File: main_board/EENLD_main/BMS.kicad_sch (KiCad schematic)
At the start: 20 parts, among them J201 Conn_01x02_Socket, Q201 AO3401A, SW201 SW_SPST, U201 TPS25200DRVR

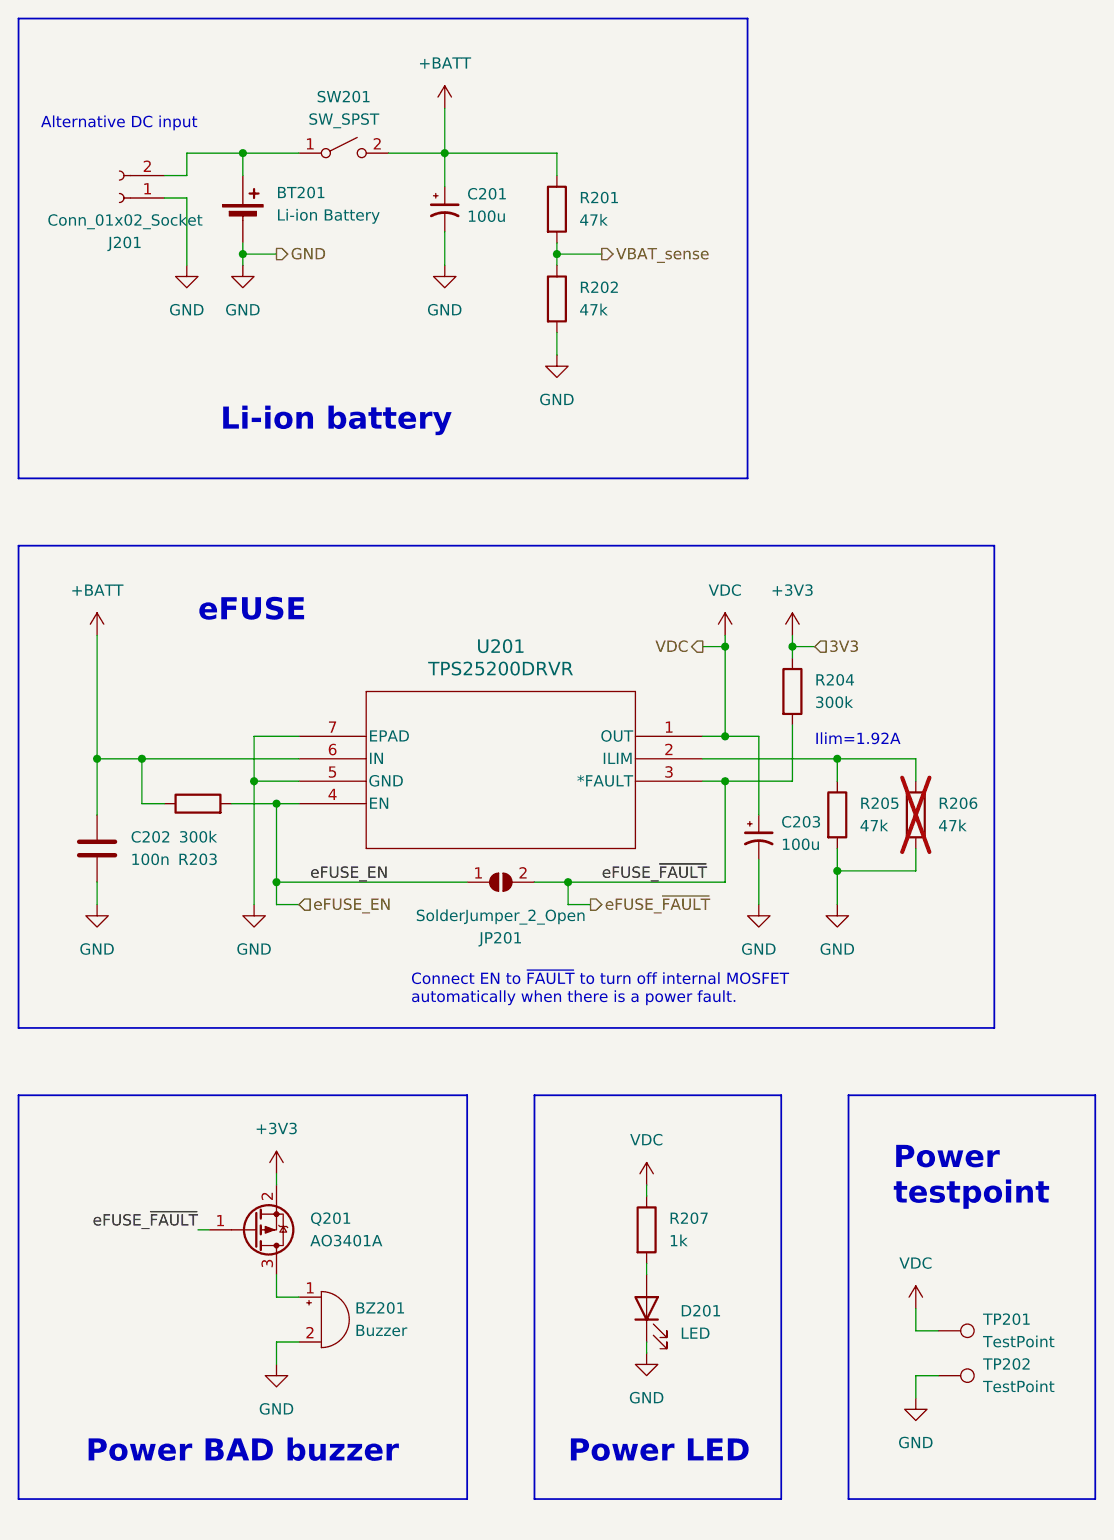
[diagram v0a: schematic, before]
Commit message: Finished PCB layout v0.1.
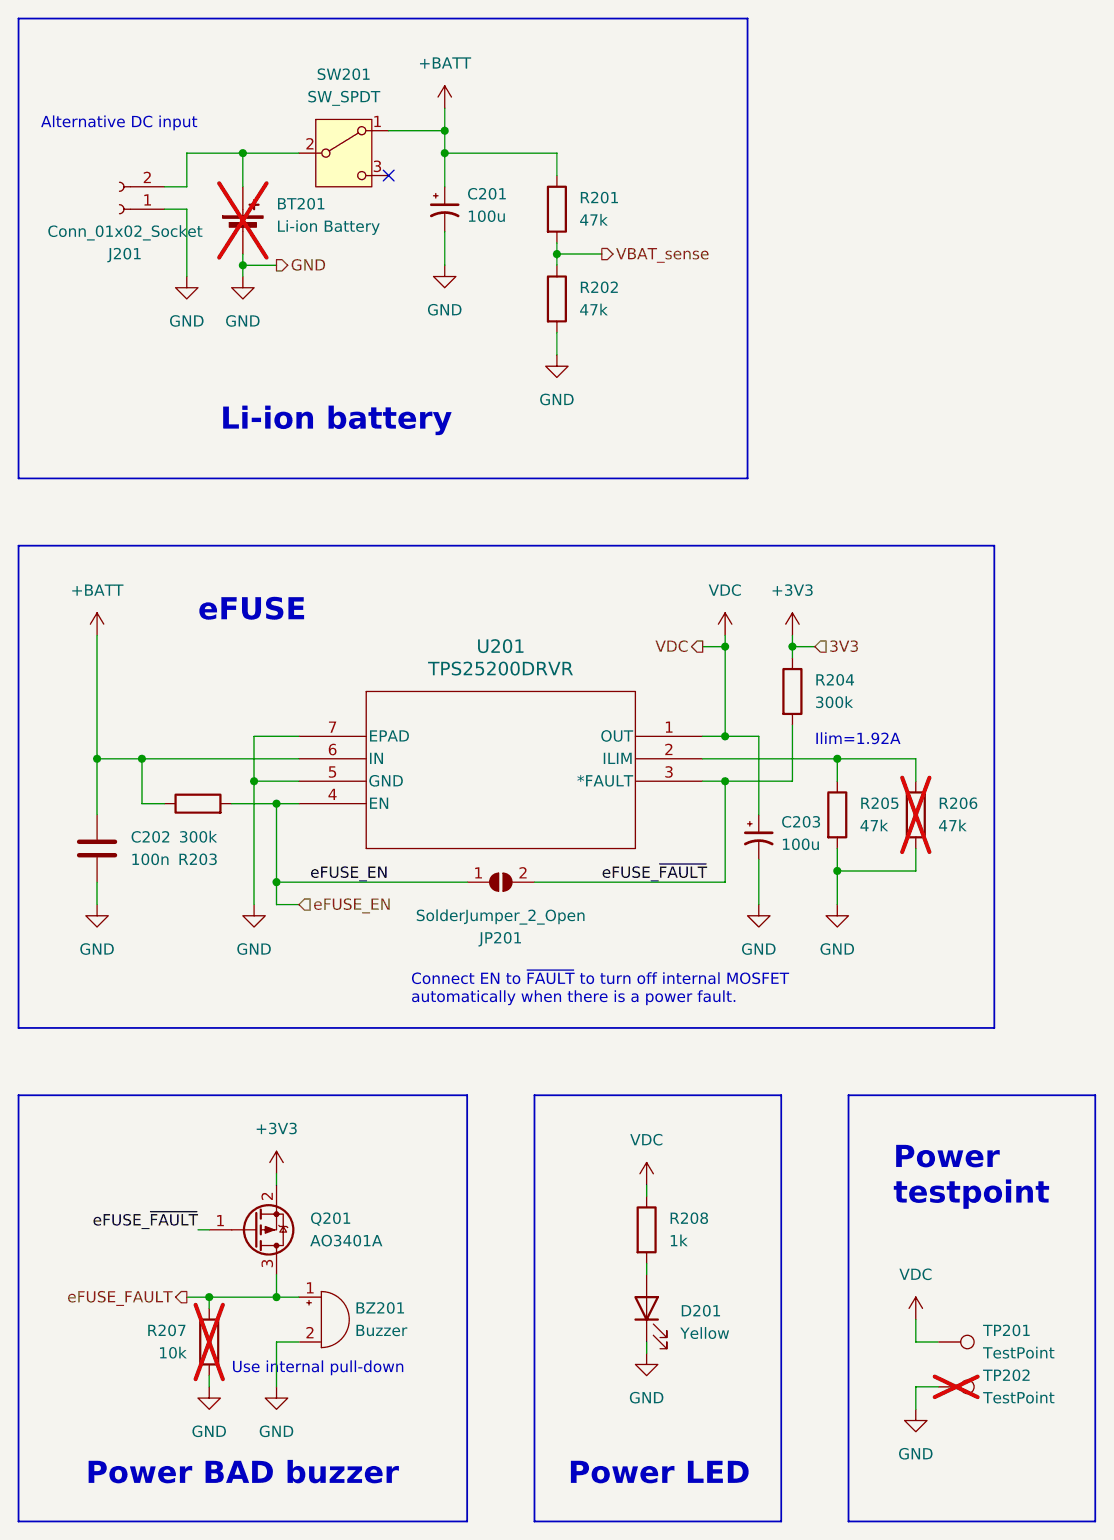
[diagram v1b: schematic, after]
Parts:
- removed SW201: SW_SPST, symbol Switch:SW_SPST
- added R207: 10k, Resistor_SMD:R_0402_1005Metric_Pad0.72x0.64mm_HandSolder, symbol Device:R
- added SW201: SW_SPDT, Button_Switch_THT:SW_Lever_1P2T_NKK_GW12LxH, symbol Switch:SW_SPDT
- BT201: now not fitted; now left out of the parts list
- BZ201: footprint Buzzer_Beeper:Buzzer_TDK_PS1240P02BT_D12.2mm_H6.5mm -> Capacitor_THT:CP_Radial_D10.0mm_P5.00mm
- C201, C203: footprint (none) -> Capacitor_THT:CP_Radial_D8.0mm_P2.50mm
- C202: footprint (none) -> Capacitor_SMD:C_0603_1608Metric_Pad1.08x0.95mm_HandSolder; LCSC (none) -> C14663
- D201: value LED -> Yellow; footprint (none) -> LED_SMD:LED_0805_2012Metric_Pad1.15x1.40mm_HandSolder; LCSC (none) -> C2296
- J201: footprint (none) -> TerminalBlock:TerminalBlock_bornier-2_P5.08mm
- JP201: footprint Jumper:SolderJumper-2_P1.3mm_Open_RoundedPad1.0x1.5mm -> Jumper:SolderJumper-2_P1.3mm_Open_Pad1.0x1.5mm
- Q201: LCSC (none) -> C15127
- R201, R202, R205: footprint Resistor_SMD:R_0603_1608Metric_Pad0.98x0.95mm_HandSolder -> Resistor_SMD:R_0402_1005Metric_Pad0.72x0.64mm_HandSolder; LCSC (none) -> C25792
- R203, R204: LCSC (none) -> C23024
- R208: renamed from R207; footprint (none) -> Resistor_SMD:R_0603_1608Metric_Pad0.98x0.95mm_HandSolder; LCSC (none) -> C21190
- TP201: footprint (none) -> TestPoint:TestPoint_THTPad_D1.5mm_Drill0.7mm
- TP202: footprint (none) -> TestPoint:TestPoint_THTPad_D1.5mm_Drill0.7mm; now not fitted; now left out of the parts list
- U201: LCSC (none) -> C128401
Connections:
- net +BATT: now also SW201.1 (A)
- net GND: now also R207.2
- net eFUSE_FAULT: now reaches BZ201.1 (+), Q201.3 (D)
- net eFUSE_FAULT: now also R207.1
- net at BT201.1 (+), J201.2 (Pin_2): now also SW201.2 (B)
- no-connect marks 0 -> 1
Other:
- note added: "Use internal pull-down"
- moved on the sheet: J201, TP201

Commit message: added midi2array
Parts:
- BZ201, C201, C203, J201, JP201, SW201, TP201: now left out of the parts list
- Q201: JLCPCB Rotation Offset (none) -> 180
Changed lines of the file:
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@@
-      (effects (font (size 1.27 1.27)) hide)
-    )
-    (property "Sim.Enable" "0" (at 123.19 111.76 0)
       (effects (font (size 1.27 1.27)) hide)
     )
@@
   )
   (symbol (lib_id "Device:Buzzer") (at 55.88 168.91 0) (unit 1)
-    (in_bom yes) (on_board yes) (dnp no) (fields_autoplaced)
+    (in_bom no) (on_board yes) (dnp no) (fields_autoplaced)
     (property "Reference" "BZ201" (at 59.69 167.64 0)
       (effects (font (size 1.27 1.27)) (justify left))
@@
   )
   (symbol (lib_id "Connector:Conn_01x02_Socket") (at 33.02 43.18 180) (unit 1)
-    (in_bom yes) (on_board yes) (dnp no)
+    (in_bom no) (on_board yes) (dnp no)
     (property "Reference" "J201" (at 33.655 48.26 0)
       (effects (font (size 1.27 1.27)))
@@
   )
   (symbol (lib_id "Device:C_Polarized_Small_US") (at 105.41 114.3 0) (unit 1)
-    (in_bom yes) (on_board yes) (dnp no) (fields_autoplaced)
+    (in_bom no) (on_board yes) (dnp no) (fields_autoplaced)
     (property "Reference" "C203" (at 107.95 112.5982 0)
       (effects (font (size 1.27 1.27)) (justify left))
@@
   )
   (symbol (lib_id "Connector:TestPoint") (at 125.73 171.45 270) (unit 1)
-    (in_bom yes) (on_board yes) (dnp no) (fields_autoplaced)
+    (in_bom no) (on_board yes) (dnp no) (fields_autoplaced)
     (property "Reference" "TP201" (at 130.81 170.18 90)
       (effects (font (size 1.27 1.27)) (justify left))
@@
   )
   (symbol (lib_id "Jumper:SolderJumper_2_Open") (at 76.2 119.38 0) (unit 1)
-    (in_bom yes) (on_board yes) (dnp no)
+    (in_bom no) (on_board yes) (dnp no)
     (property "Reference" "JP201" (at 76.2 125.73 0)
       (effects (font (size 1.27 1.27)))
@@
   )
   (symbol (lib_id "Device:C_Polarized_Small_US") (at 69.85 43.18 0) (unit 1)
-    (in_bom yes) (on_board yes) (dnp no) (fields_autoplaced)
+    (in_bom no) (on_board yes) (dnp no) (fields_autoplaced)
     (property "Reference" "C201" (at 72.39 41.4782 0)
       (effects (font (size 1.27 1.27)) (justify left))
@@
   )
   (symbol (lib_id "Switch:SW_SPDT") (at 58.42 36.83 0) (unit 1)
-    (in_bom yes) (on_board yes) (dnp no)
+    (in_bom no) (on_board yes) (dnp no)
     (property "Reference" "SW201" (at 58.42 27.94 0)
       (effects (font (size 1.27 1.27)))
@@
       (effects (font (size 1.27 1.27)) (justify left) hide)
     )
-    (property "JLCPCB Rotation Offset" "" (at 48.26 158.75 0)
-      (effects (font (size 1.27 1.27)) hide)
-    )
+    (property "JLCPCB Rotation Offset" "180" (at 48.26 158.75 0)
+      (effects (font (size 1.27 1.27)) hide)
+    )
